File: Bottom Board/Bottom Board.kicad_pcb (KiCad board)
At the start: 2 copper layers, 88.9 x 27.9 mm, 5 parts

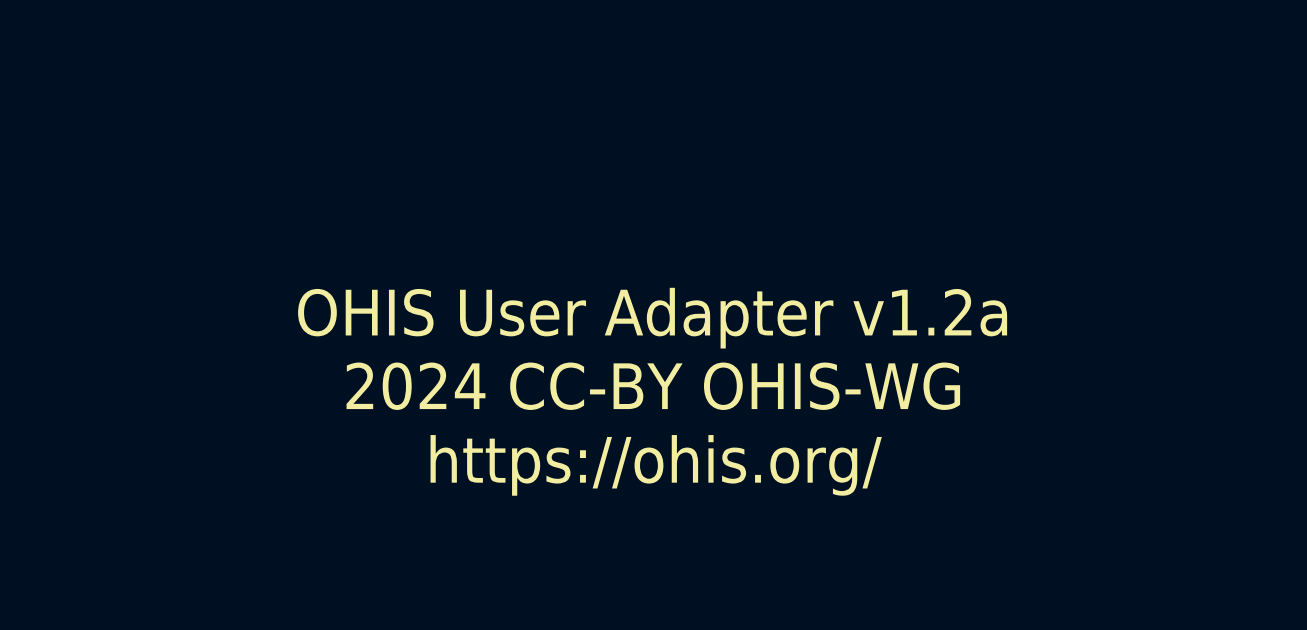
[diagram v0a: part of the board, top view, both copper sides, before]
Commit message: Halibut ordering next batch. Upping version on top/bottom to v1.3a. KiCAD 8.0
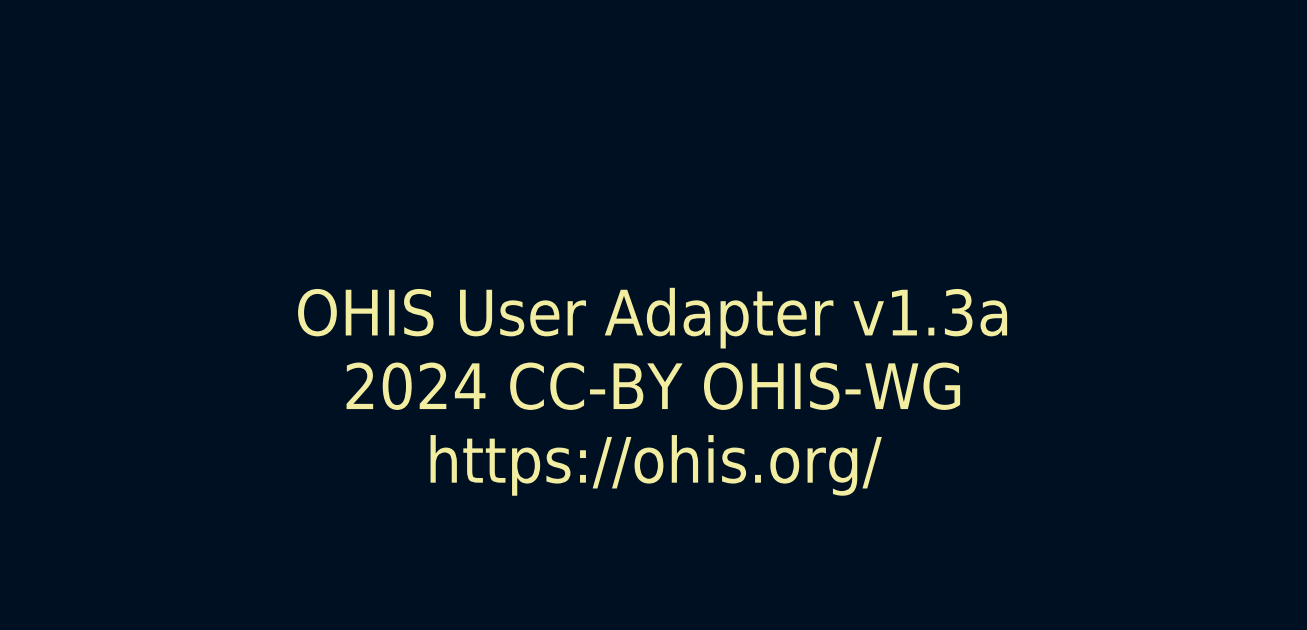
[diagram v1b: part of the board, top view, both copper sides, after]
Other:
- board text added: "OHIS User Adapter v1.3a 2024 CC-BY OHIS-WG https://ohis.org/"
- board text removed: "OHIS User Adapter v1.2a 2024 CC-BY OHIS-WG https://ohis.org/"
